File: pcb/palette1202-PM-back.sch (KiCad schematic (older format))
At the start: 9 parts

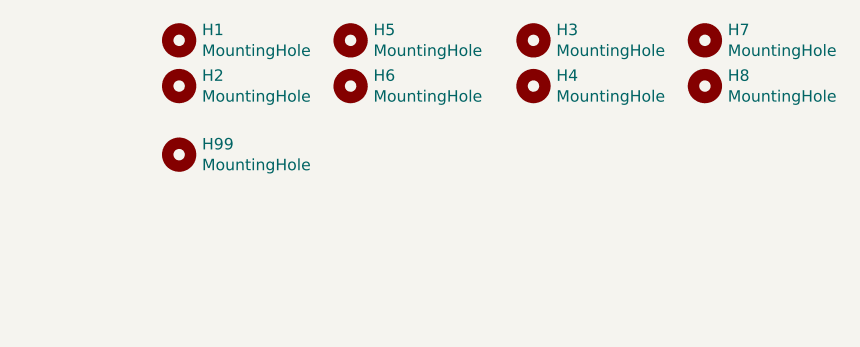
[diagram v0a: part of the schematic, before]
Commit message: updated back panel
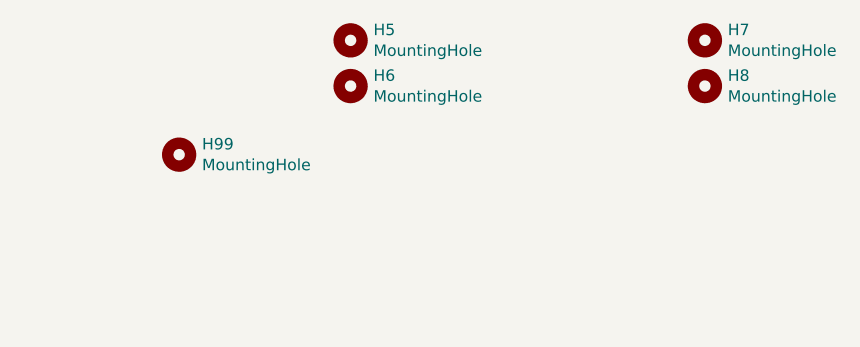
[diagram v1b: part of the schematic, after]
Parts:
- removed H1, H2, H3, H4: MountingHole, nilgiri:M2_vis, symbol Mechanical:MountingHole
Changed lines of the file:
@@
 EESchema Schematic File Version 4
-LIBS:nilgiri_back-cache
 EELAYER 30 0
 EELAYER END
@@
 NoConn ~ 700  6400
 NoConn ~ -1200 3850
-$Comp
-L Mechanical:MountingHole H2
-U 1 1 5DB4A9FD
-P 4050 3400
-F 0 "H2" H 4150 3446 50  0000 L CNN
-F 1 "MountingHole" H 4150 3355 50  0000 L CNN
-F 2 "nilgiri:M2_vis" H 4050 3400 50  0001 C CNN
-F 3 "~" H 4050 3400 50  0001 C CNN
-	1    4050 3400
-	1    0    0    -1
-$EndComp
-$Comp
-L Mechanical:MountingHole H6
-U 1 1 5DB4B5D0
-P 4800 3400
-F 0 "H6" H 4900 3446 50  0000 L CNN
-F 1 "MountingHole" H 4900 3355 50  0000 L CNN
-F 2 "nilgiri:M2_vis" H 4800 3400 50  0001 C CNN
-F 3 "~" H 4800 3400 50  0001 C CNN
-	1    4800 3400
-	1    0    0    -1
-$EndComp
-$Comp
-L Mechanical:MountingHole H1
-U 1 1 5DB4B94A
-P 4050 3200
-F 0 "H1" H 4150 3246 50  0000 L CNN
-F 1 "MountingHole" H 4150 3155 50  0000 L CNN
-F 2 "nilgiri:M2_vis" H 4050 3200 50  0001 C CNN
-F 3 "~" H 4050 3200 50  0001 C CNN
-	1    4050 3200
-	1    0    0    -1
-$EndComp
-$Comp
-L Mechanical:MountingHole H5
-U 1 1 5DB4C3DF
-P 4800 3200
-F 0 "H5" H 4900 3246 50  0000 L CNN
-F 1 "MountingHole" H 4900 3155 50  0000 L CNN
-F 2 "nilgiri:M2_vis" H 4800 3200 50  0001 C CNN
-F 3 "~" H 4800 3200 50  0001 C CNN
-	1    4800 3200
-	1    0    0    -1
-$EndComp
-$Comp
-L Mechanical:MountingHole H3
-U 1 1 5DB4C79D
-P 5600 3200
-F 0 "H3" H 5700 3246 50  0000 L CNN
-F 1 "MountingHole" H 5700 3155 50  0000 L CNN
-F 2 "nilgiri:M2_vis" H 5600 3200 50  0001 C CNN
-F 3 "~" H 5600 3200 50  0001 C CNN
-	1    5600 3200
-	1    0    0    -1
-$EndComp
 $Comp
 L Mechanical:MountingHole H7
@@
 $EndComp
 $Comp
-L Mechanical:MountingHole H4
-U 1 1 5DB4CF1F
-P 5600 3400
-F 0 "H4" H 5700 3446 50  0000 L CNN
-F 1 "MountingHole" H 5700 3355 50  0000 L CNN
-F 2 "nilgiri:M2_vis" H 5600 3400 50  0001 C CNN
-F 3 "~" H 5600 3400 50  0001 C CNN
-	1    5600 3400
-	1    0    0    -1
-$EndComp
-$Comp
 L Mechanical:MountingHole H99
 U 1 1 5DBCB9AA
@@
 	1    0    0    -1
 $EndComp
+$Comp
+L Mechanical:MountingHole H5
+U 1 1 5DB4C3DF
+P 4800 3200
+F 0 "H5" H 4900 3246 50  0000 L CNN
+F 1 "MountingHole" H 4900 3155 50  0000 L CNN
+F 2 "nilgiri:M2_vis" H 4800 3200 50  0001 C CNN
+F 3 "~" H 4800 3200 50  0001 C CNN
+	1    4800 3200
+	1    0    0    -1
+$EndComp
+$Comp
+L Mechanical:MountingHole H6
+U 1 1 5DB4B5D0
+P 4800 3400
+F 0 "H6" H 4900 3446 50  0000 L CNN
+F 1 "MountingHole" H 4900 3355 50  0000 L CNN
+F 2 "nilgiri:M2_vis" H 4800 3400 50  0001 C CNN
+F 3 "~" H 4800 3400 50  0001 C CNN
+	1    4800 3400
+	1    0    0    -1
+$EndComp
